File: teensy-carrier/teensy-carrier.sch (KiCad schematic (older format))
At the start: 3 parts, among them J1 Conn_01x02_Male, J2 Conn_01x15_Female, U1 Teensy3.2

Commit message: work on teensy-carrier
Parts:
- added J3: Conn_01x02_Female, Connector_PinHeader_2.54mm:PinHeader_1x02_P2.54mm_Horizontal, symbol Connector:Conn_01x02_Female
- added U2: LM1084-5.0, Package_TO_SOT_SMD:TO-263-3_TabPin2, symbol Regulator_Linear:LM1084-5.0
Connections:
- net +5V: now also J3.2 (Pin_2), U2.2 (VO); no longer J1.2 (Pin_2)
- net GND: now also J3.1 (Pin_1), U2.1 (GND)
- new net: J1.2 (Pin_2), U2.3 (VI)
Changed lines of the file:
@@
-$EndComp
-$Comp
-L power:+5V #PWR0101
-U 1 1 5DE57F92
-P 6350 1450
-F 0 "#PWR0101" H 6350 1300 50  0001 C CNN
-F 1 "+5V" H 6365 1623 50  0000 C CNN
-F 2 "" H 6350 1450 50  0001 C CNN
-F 3 "" H 6350 1450 50  0001 C CNN
-	1    6350 1450
-	1    0    0    -1
 $EndComp
 $Comp
@@
 $EndComp
 Wire Wire Line
-	6350 1450 6350 1550
-Wire Wire Line
 	4550 4350 4750 4350
 Wire Wire Line
@@
 Wire Wire Line
 	6350 1650 6350 1750
-Wire Wire Line
-	6250 1550 6350 1550
 Wire Wire Line
 	2550 4050 2000 4050
@@
 Text Label 2000 3150 0    50   ~ 0
 LAT
+$Comp
+L Regulator_Linear:LM1084-5.0 U2
+U 1 1 5DE7073C
+P 7100 1550
+F 0 "U2" H 7100 1792 50  0000 C CNN
+F 1 "LM1084-5.0" H 7100 1701 50  0000 C CNN
+F 2 "Package_TO_SOT_SMD:TO-263-3_TabPin2" H 7100 1800 50  0001 C CIN
+F 3 "http://www.ti.com/lit/ds/symlink/lm1084.pdf" H 7100 1550 50  0001 C CNN
+	1    7100 1550
+	1    0    0    -1
+$EndComp
+Wire Wire Line
+	6250 1550 6800 1550
+$Comp
+L Connector:Conn_01x02_Female J3
+U 1 1 5DE734F8
+P 8100 1650
+F 0 "J3" H 7992 1325 50  0000 C CNN
+F 1 "Conn_01x02_Female" H 7992 1416 50  0000 C CNN
+F 2 "Connector_PinHeader_2.54mm:PinHeader_1x02_P2.54mm_Horizontal" H 8100 1650 50  0001 C CNN
+F 3 "~" H 8100 1650 50  0001 C CNN
+	1    8100 1650
+	1    0    0    1
+$EndComp
+Wire Wire Line
+	7400 1550 7500 1550
+$Comp
+L power:GND #PWR0101
+U 1 1 5DE75581
+P 7100 1900
+F 0 "#PWR0101" H 7100 1650 50  0001 C CNN
+F 1 "GND" H 7105 1727 50  0000 C CNN
+F 2 "" H 7100 1900 50  0001 C CNN
+F 3 "" H 7100 1900 50  0001 C CNN
+	1    7100 1900
+	1    0    0    -1
+$EndComp
+$Comp
+L power:GND #PWR0109
+U 1 1 5DE75B54
+P 7800 1750
+F 0 "#PWR0109" H 7800 1500 50  0001 C CNN
+F 1 "GND" H 7805 1577 50  0000 C CNN
+F 2 "" H 7800 1750 50  0001 C CNN
+F 3 "" H 7800 1750 50  0001 C CNN
+	1    7800 1750
+	1    0    0    -1
+$EndComp
+Wire Wire Line
+	7900 1650 7800 1650
+Wire Wire Line
+	7800 1650 7800 1750
+Wire Wire Line
+	7100 1850 7100 1900
+$Comp
+L power:+5V #PWR0110
+U 1 1 5DE77513
+P 7500 1450
+F 0 "#PWR0110" H 7500 1300 50  0001 C CNN
+F 1 "+5V" H 7515 1623 50  0000 C CNN
+F 2 "" H 7500 1450 50  0001 C CNN
+F 3 "" H 7500 1450 50  0001 C CNN
+	1    7500 1450
+	1    0    0    -1
+$EndComp
+Wire Wire Line
+	7500 1450 7500 1550
+Connection ~ 7500 1550
+Wire Wire Line
+	7500 1550 7900 1550
 $EndSCHEMATC

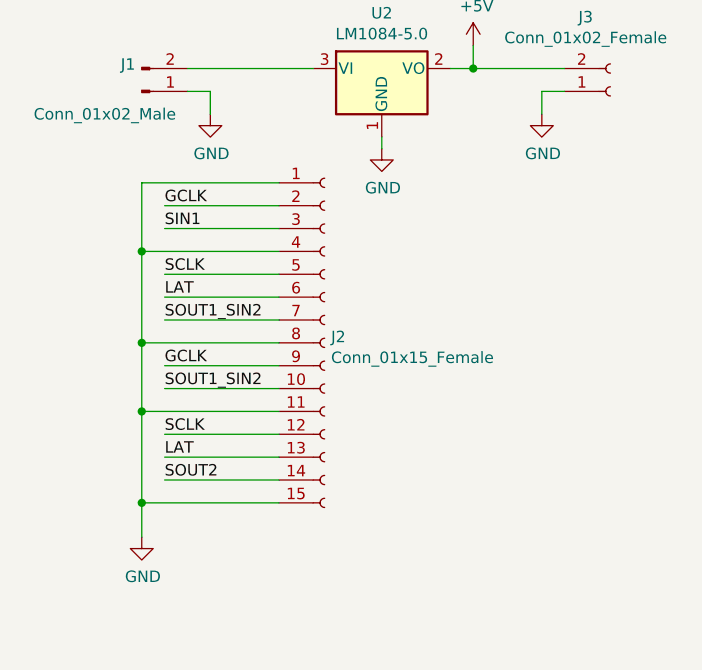
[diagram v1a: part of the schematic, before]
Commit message: fix reversed wiring
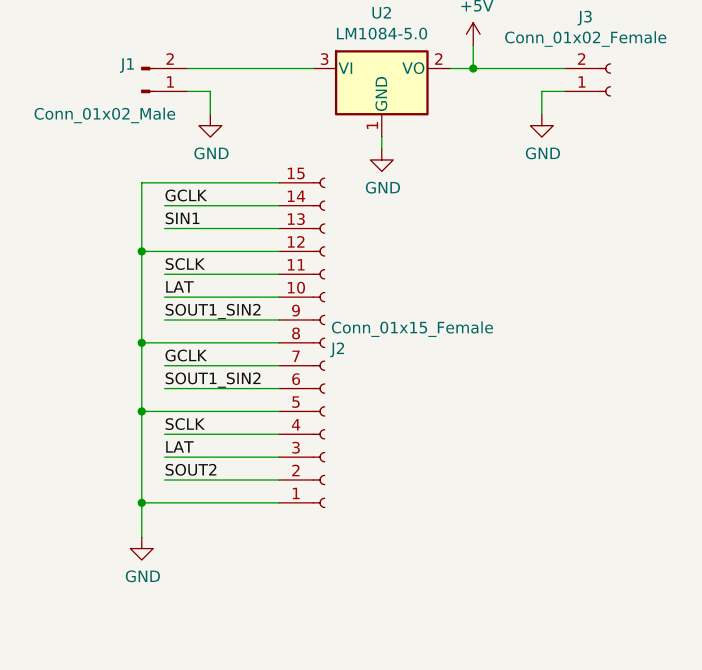
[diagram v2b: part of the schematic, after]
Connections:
- net GCLK: now also J2.14 (Pin_14), J2.7 (Pin_7); no longer J2.2 (Pin_2), J2.9 (Pin_9)
- net GND: now also J2.12 (Pin_12), J2.5 (Pin_5); no longer J2.11 (Pin_11), J2.4 (Pin_4)
- net LAT: now also J2.10 (Pin_10), J2.3 (Pin_3); no longer J2.13 (Pin_13), J2.6 (Pin_6)
- net SCLK: now also J2.11 (Pin_11), J2.4 (Pin_4); no longer J2.12 (Pin_12), J2.5 (Pin_5)
- net SIN1: now also J2.13 (Pin_13); no longer J2.3 (Pin_3)
- net SOUT1_SIN2: now also J2.6 (Pin_6), J2.9 (Pin_9); no longer J2.10 (Pin_10), J2.7 (Pin_7)
- net SOUT2: now also J2.2 (Pin_2); no longer J2.14 (Pin_14)
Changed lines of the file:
@@
 F 3 "~" H 6850 2750 50  0001 C CNN
 	1    6850 2750
-	1    0    0    -1
+	1    0    0    1
 $EndComp
 Wire Wire Line

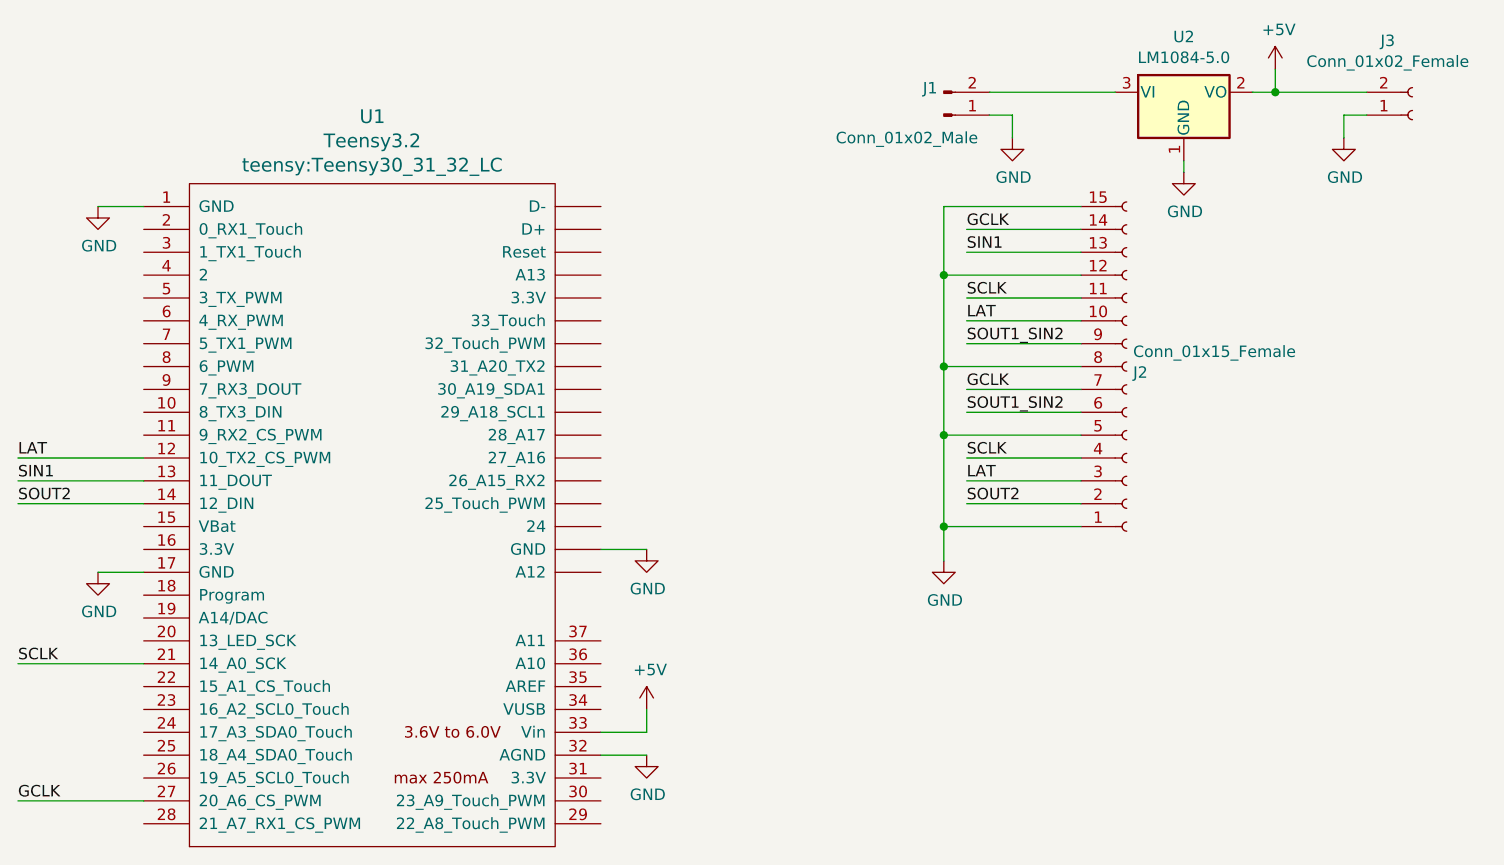
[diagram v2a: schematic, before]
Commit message: fix pin ordering, use terminal blocks instead of pin headers for power entry/supply
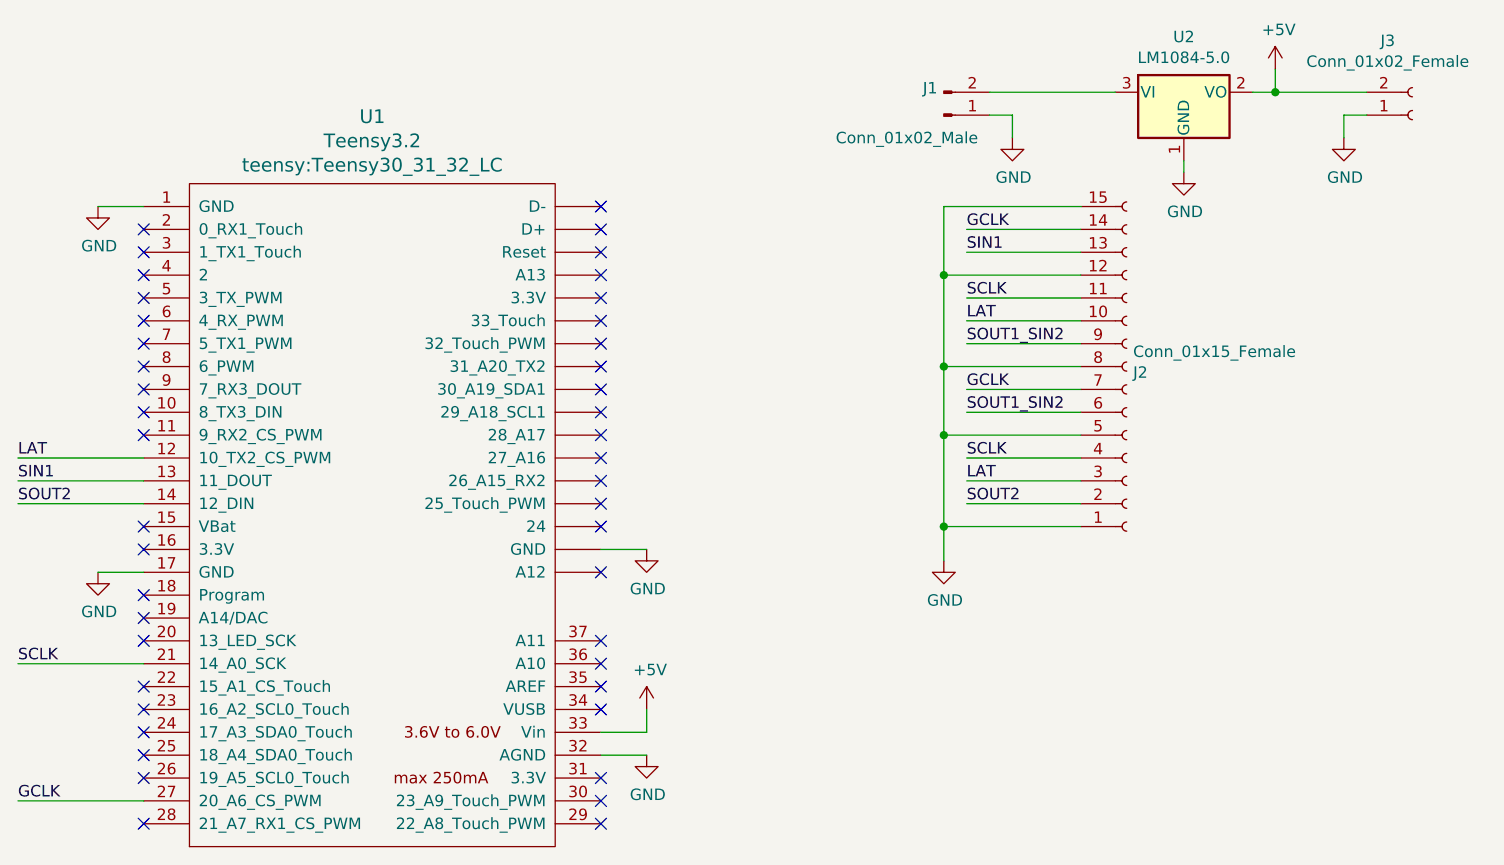
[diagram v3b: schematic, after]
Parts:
- J1, J3: footprint Connector_PinHeader_2.54mm:PinHeader_1x02_P2.54mm_Horizontal -> teensy:TerminalBlock_DECA-MB312-254-2
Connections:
- no-connect marks 0 -> 44
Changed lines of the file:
@@
 F 0 "J1" H 6022 1532 50  0000 R CNN
 F 1 "Conn_01x02_Male" H 6200 1750 50  0000 R CNN
-F 2 "Connector_PinHeader_2.54mm:PinHeader_1x02_P2.54mm_Horizontal" H 6050 1650 50  0001 C CNN
+F 2 "teensy:TerminalBlock_DECA-MB312-254-2" H 6050 1650 50  0001 C CNN
 F 3 "~" H 6050 1650 50  0001 C CNN
 	1    6050 1650
@@
 F 0 "J3" H 7992 1325 50  0000 C CNN
 F 1 "Conn_01x02_Female" H 7992 1416 50  0000 C CNN
-F 2 "Connector_PinHeader_2.54mm:PinHeader_1x02_P2.54mm_Horizontal" H 8100 1650 50  0001 C CNN
+F 2 "teensy:TerminalBlock_DECA-MB312-254-2" H 8100 1650 50  0001 C CNN
 F 3 "~" H 8100 1650 50  0001 C CNN
 	1    8100 1650
@@
 Wire Wire Line
 	7500 1550 7900 1550
+NoConn ~ 4550 3650
+NoConn ~ 4550 3950
+NoConn ~ 4550 4050
+NoConn ~ 4550 4150
+NoConn ~ 4550 4250
+NoConn ~ 4550 4550
+NoConn ~ 4550 4650
+NoConn ~ 4550 4750
+NoConn ~ 4550 2050
+NoConn ~ 4550 2150
+NoConn ~ 4550 2250
+NoConn ~ 4550 2350
+NoConn ~ 4550 2450
+NoConn ~ 4550 2550
+NoConn ~ 4550 2650
+NoConn ~ 4550 2750
+NoConn ~ 4550 2850
+NoConn ~ 4550 2950
+NoConn ~ 4550 3050
+NoConn ~ 4550 3150
+NoConn ~ 4550 3250
+NoConn ~ 4550 3350
+NoConn ~ 4550 3450
+NoConn ~ 2550 2150
+NoConn ~ 2550 2250
+NoConn ~ 2550 2350
+NoConn ~ 2550 2450
+NoConn ~ 2550 2550
+NoConn ~ 2550 2650
+NoConn ~ 2550 2750
+NoConn ~ 2550 2850
+NoConn ~ 2550 2950
+NoConn ~ 2550 3050
+NoConn ~ 2550 3450
+NoConn ~ 2550 3550
+NoConn ~ 2550 3750
+NoConn ~ 2550 3850
+NoConn ~ 2550 3950
+NoConn ~ 2550 4150
+NoConn ~ 2550 4250
+NoConn ~ 2550 4350
+NoConn ~ 2550 4450
+NoConn ~ 2550 4550
+NoConn ~ 2550 4750
 $EndSCHEMATC
